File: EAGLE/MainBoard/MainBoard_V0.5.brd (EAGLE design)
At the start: 36.8 x 104.1 mm, 34 parts, among them IC1 CEM3340

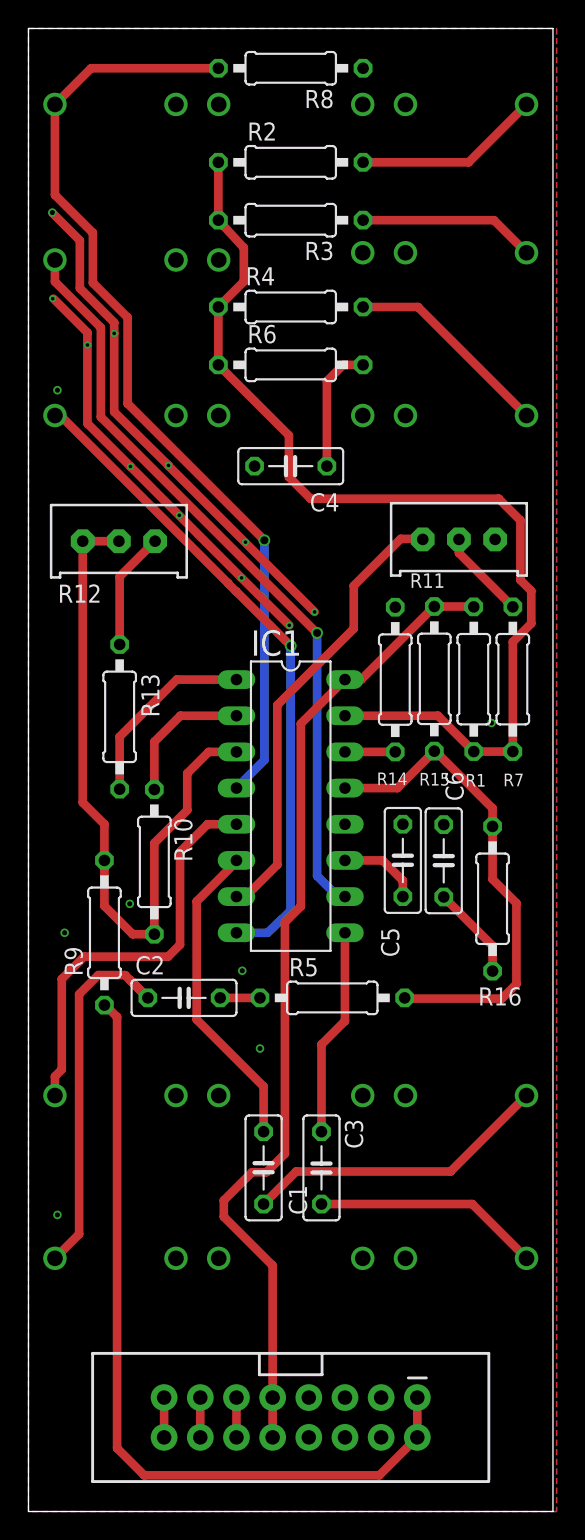
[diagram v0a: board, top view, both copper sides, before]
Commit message: Add 5V Reg. CAM Files
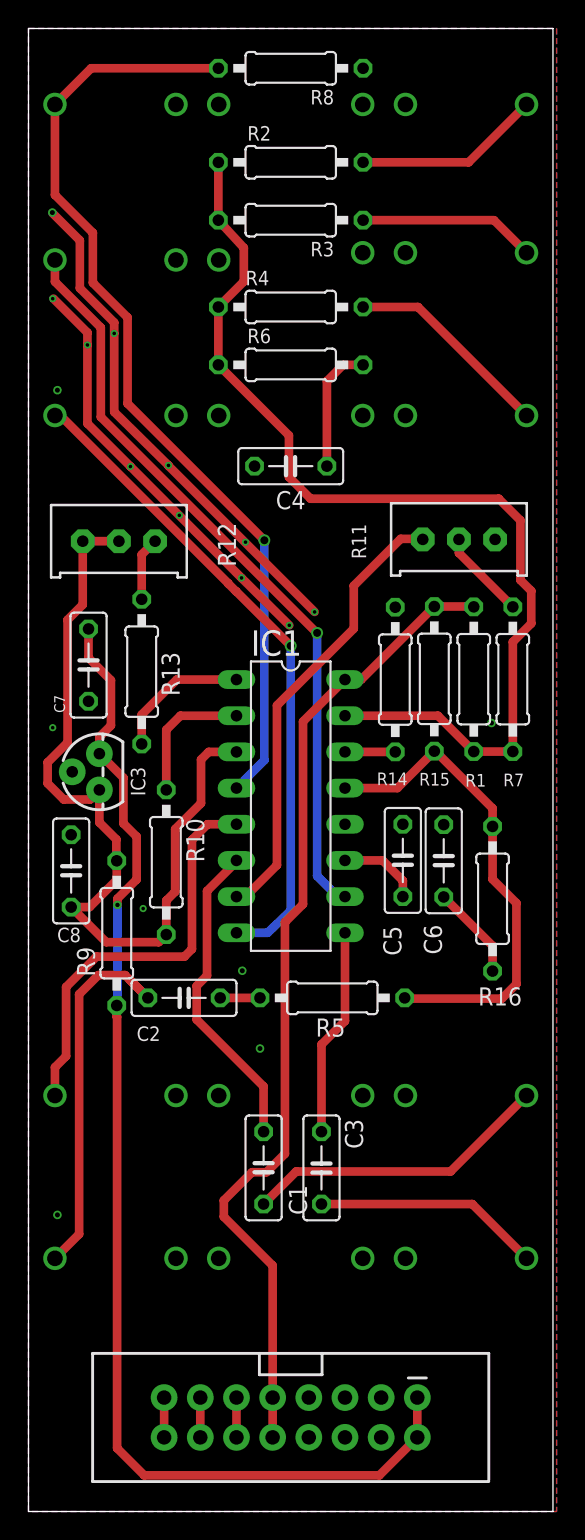
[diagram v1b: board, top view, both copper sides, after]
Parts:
- added C7: 0.33μF, rcl:C050-025X075
- added C8: 0.1μF, rcl:C050-025X075
- added IC3: L79L05, SparkFun-IC-Power:TO-92
- moved R13 3.53 mm to (7.95, 59.0)
- moved R9 0.86 mm to (6.20, 40.6)
- moved R10 0.84 mm to (9.68, 45.6)
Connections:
- net -12V: now also C7.2, IC3.3
- net GND: now also C7.1, C8.2, IC3.2
- net N$15: now also C8.1, IC3.1
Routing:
- net -12V: track 57.3 -> 86.0 mm, vias 0 -> 1
- net N$15: track 49.4 -> 59.7 mm
- net N$11: track 8.28 -> 4.47 mm
- net N$8: track 13.5 -> 9.73 mm

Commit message: Update Power IC Add Optional Component Clarification
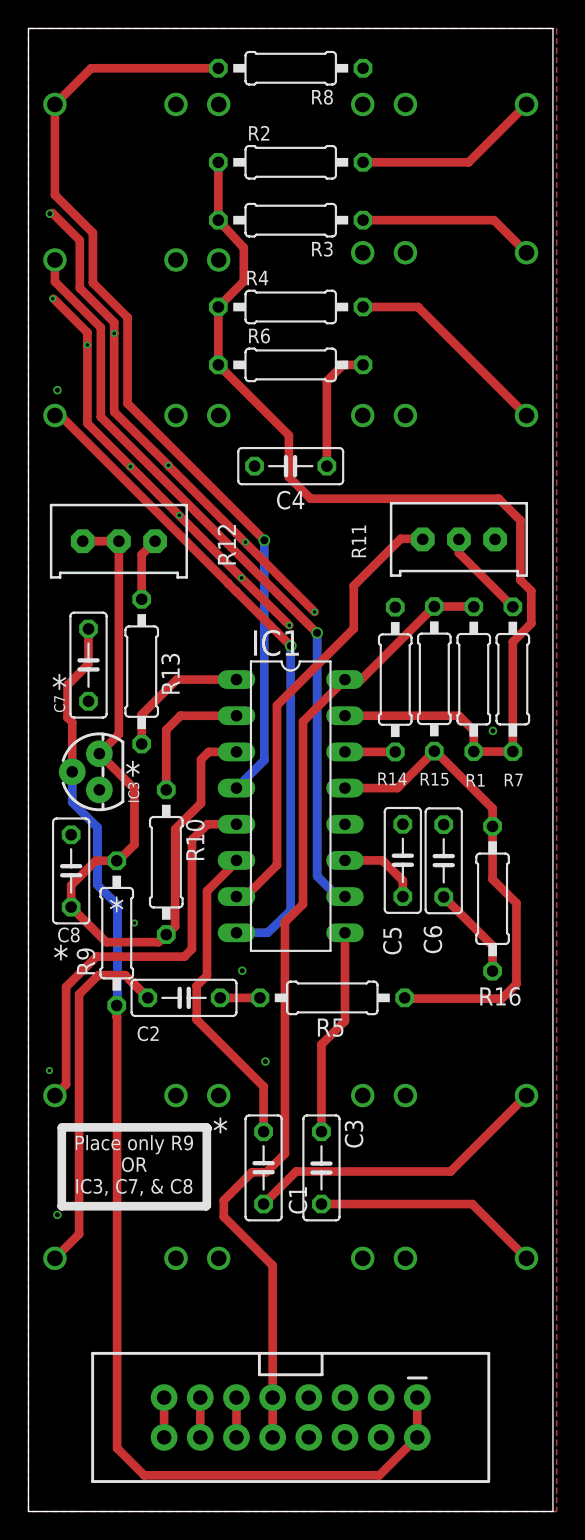
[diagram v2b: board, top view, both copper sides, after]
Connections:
- net -12V: now also IC3.2; no longer IC3.3
- net GND: now also IC3.1; no longer IC3.2
- net N$15: now also IC3.3; no longer IC3.1
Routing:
- net N$15: track 59.7 -> 56.5 mm
- net FCTL: track 73.0 -> 73.9 mm
- net -12V: track 86.0 -> 85.4 mm, vias 1 -> 0
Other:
- board text added: "*"
- board text added: "Place only R9 OR IC3, C7, & C8"
